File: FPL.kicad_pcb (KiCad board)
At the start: 4 copper layers, 100 x 99.8 mm, 62 parts, among them J1 DM3CS-SF, J10 PINHD_1x2_Male, J18 PINHD_1x5_Male, J19 PINHD_1x5_Male, J2 CX90BW1-24P1, J20 PINHD_1x5_Male, J21 PINHD_1x5_Male, J22 PINHD_1x5_Male, J3 PINHD_1x6_Male, J4 2041411-1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

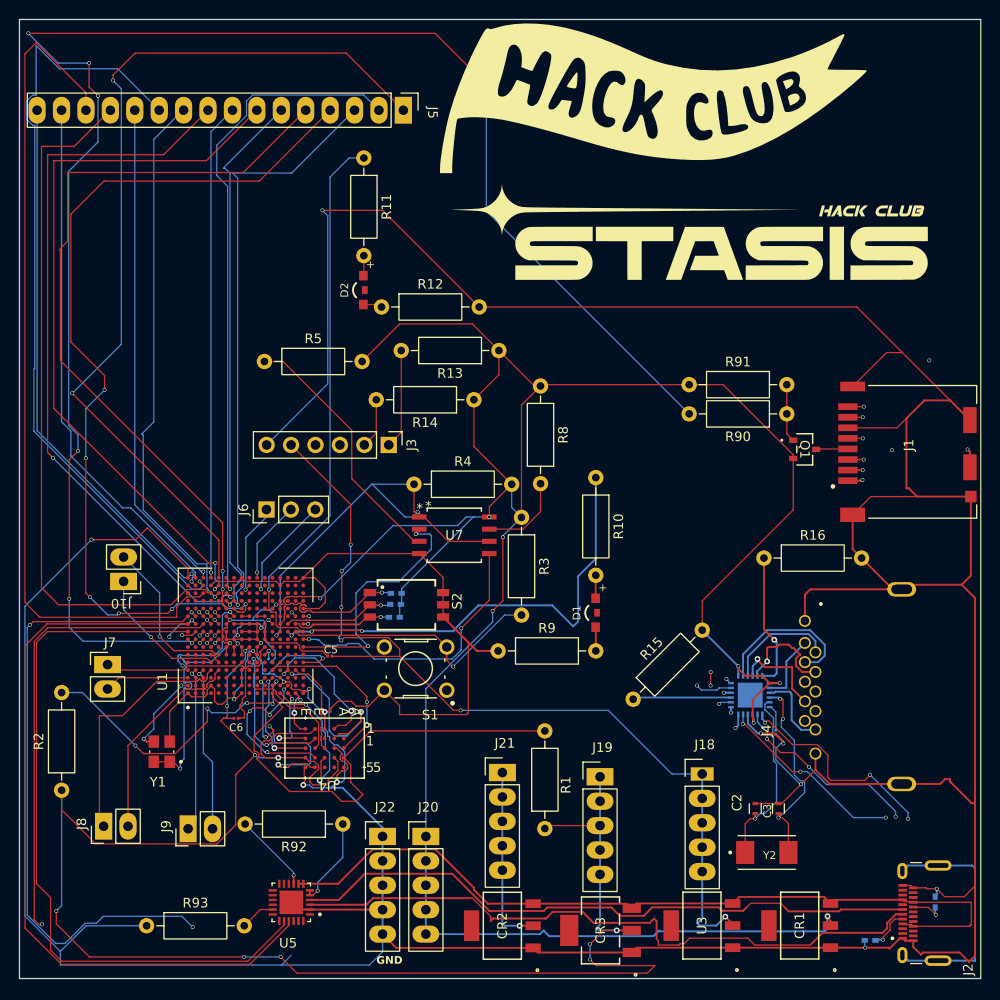
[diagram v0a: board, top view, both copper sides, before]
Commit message: BOM updates and readme updates , mainanence, code
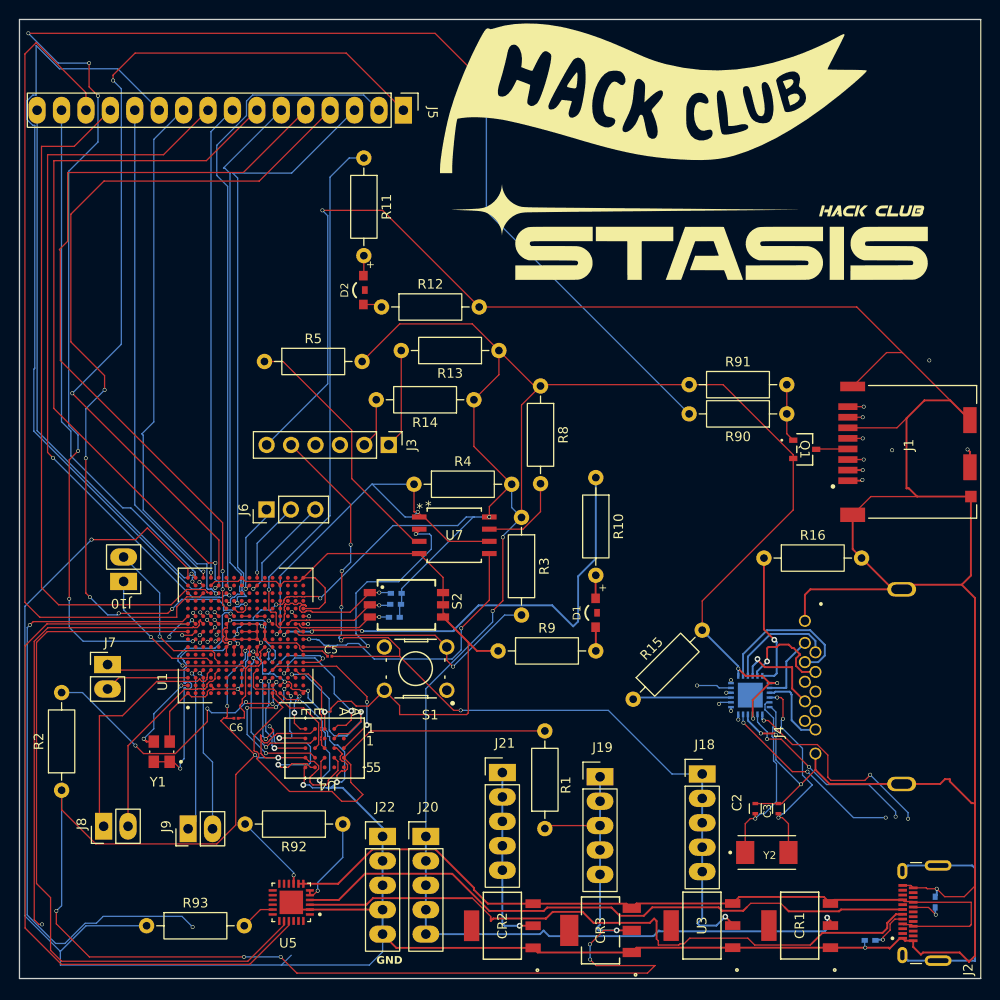
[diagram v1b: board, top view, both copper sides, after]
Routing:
- net PT56A: track 208.2 -> 214.2 mm, vias 4 -> 2
- net GND: track 631.8 -> 626.5 mm
- net PT47A: track 324.2 -> 328.4 mm
- net 3V3: track 305.1 -> 302.6 mm
- net 1V8: track 186.4 -> 188.0 mm
- net PT49A: track 221.1 -> 222.6 mm
- net Net-(U1C-PR14D): track 76.2 -> 74.8 mm
- net PT35B: track 182.4 -> 183.7 mm
- net Net-(U1C-PR20A): track 93.6 -> 94.6 mm
- net PT49B: track 225.5 -> 224.6 mm
- net Net-(U1G-DONE): track 48.6 -> 49.4 mm
- net VCC: track 16.4 -> 15.8 mm
- net PT44B: track 175.6 -> 175.1 mm
- net VCCAUX: track 27.8 -> 27.3 mm
- net Net-(U1C-PR14C): track 56.8 -> 56.3 mm
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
